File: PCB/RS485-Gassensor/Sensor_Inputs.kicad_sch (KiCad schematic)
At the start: 17 parts, among them SW1 SW_DIP_x06, U3 MQ-6, U8 MQ-6

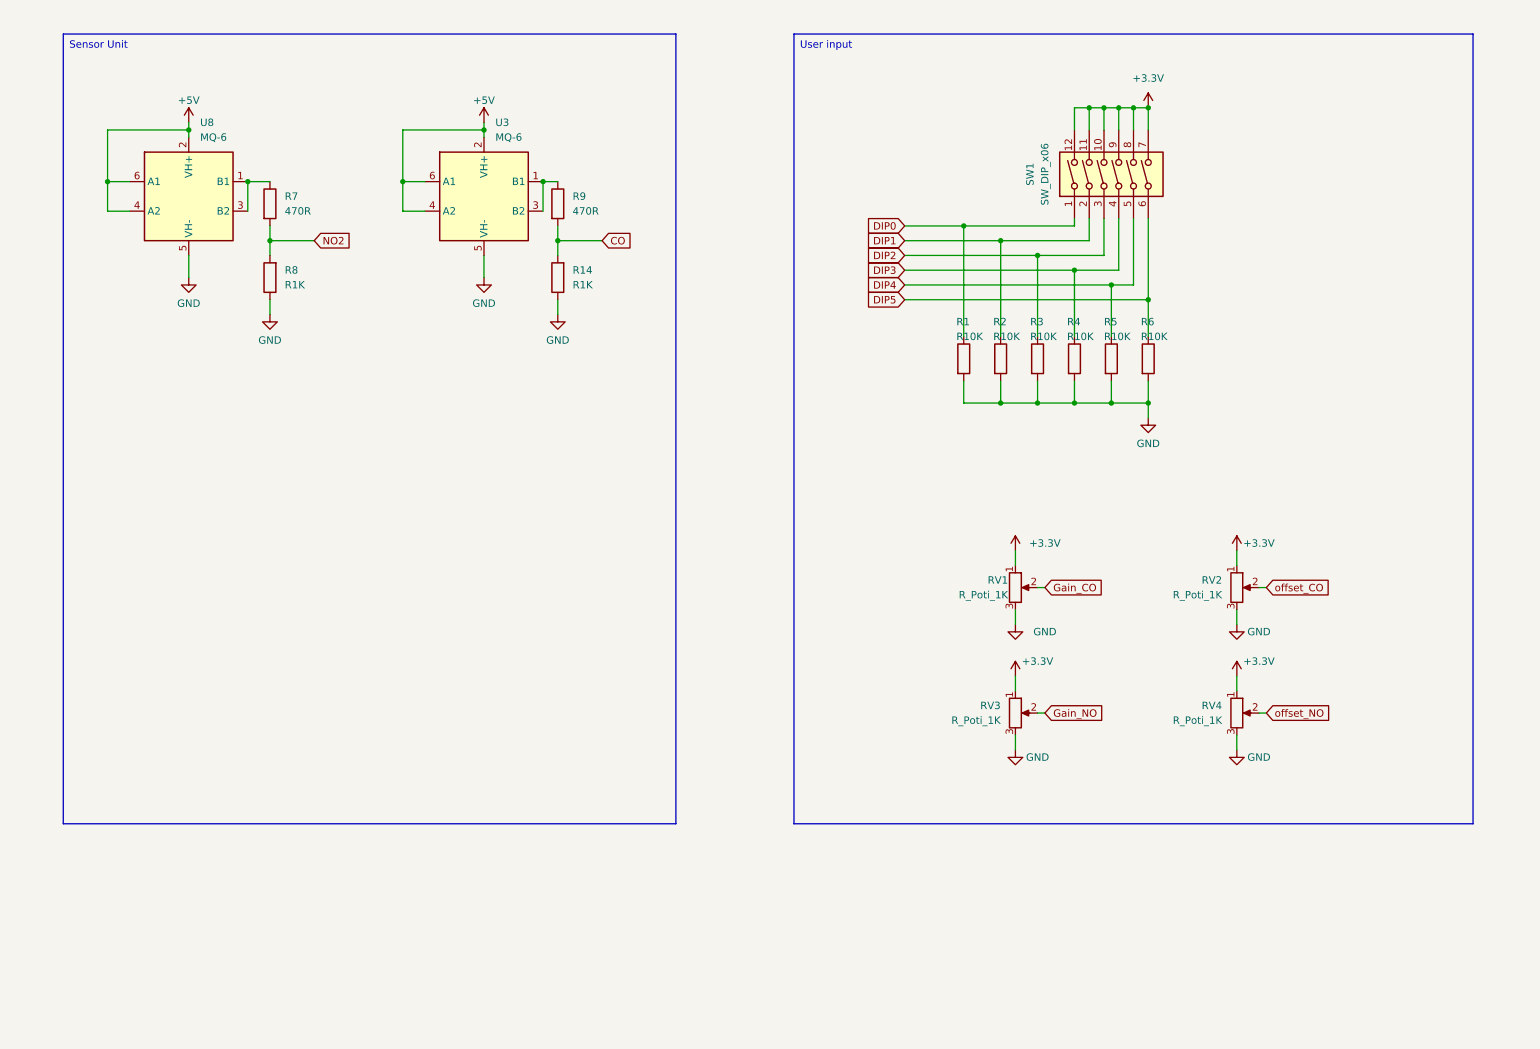
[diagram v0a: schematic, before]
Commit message: added Modbus / RS485
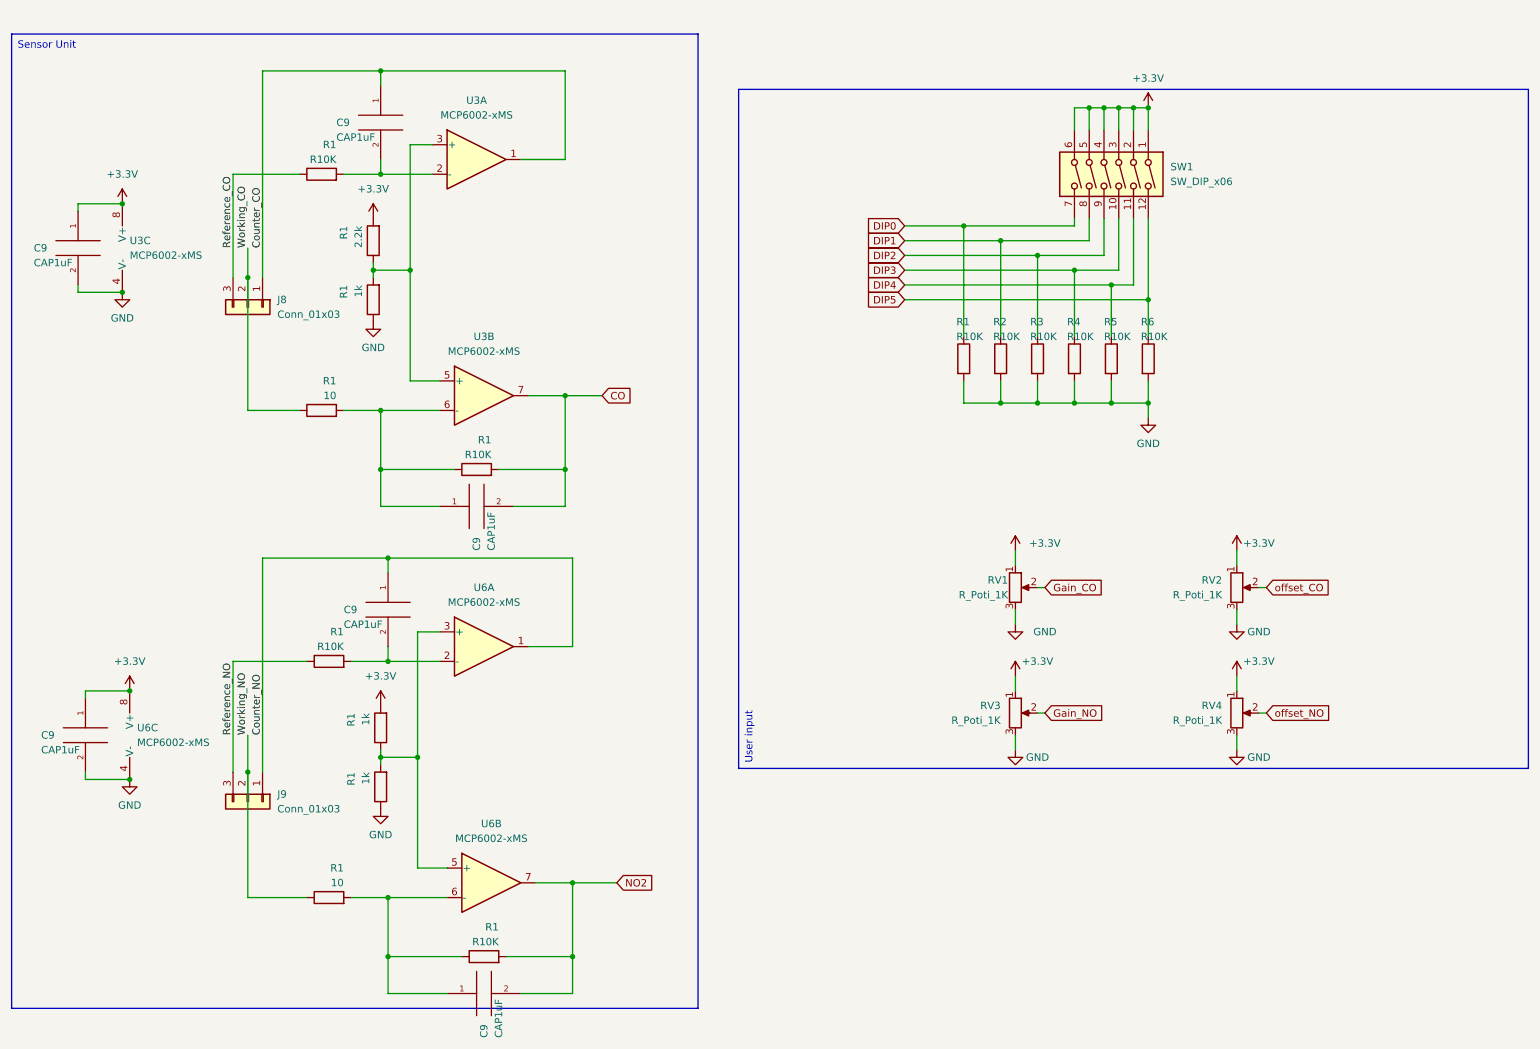
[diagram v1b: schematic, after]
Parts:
- removed R14, R8: R1K, Resistor_SMD:R_0603_1608Metric, symbol Device:R
- removed R7, R9: 470R, Resistor_SMD:R_0603_1608Metric, symbol Device:R
- removed U3, U8: MQ-6, Sensor:MQ-6, symbol Sensor_Gas:MQ-6
- added C9 (x4): CAP1uF, Capacitor_SMD:C_0603_1608Metric, symbol pspice:CAP
- added C9 (x2): CAP1uF, Capacitor_SMD:C_1206_3216Metric, symbol pspice:CAP
- added J8, J9: Conn_01x03, Connector_PinHeader_2.54mm:PinHeader_1x03_P2.54mm_Vertical, symbol Connector_Generic:Conn_01x03
- added R1 (x2): 10, Resistor_SMD:R_0603_1608Metric, symbol Device:R
- added R1 (x3): 1k, Resistor_SMD:R_0603_1608Metric, symbol Device:R
- added R1 (x4): R10K, Resistor_SMD:R_0603_1608Metric, symbol Device:R
- added R1: 2.2k, Resistor_SMD:R_0603_1608Metric, symbol Device:R
- added U3, U6: MCP6002-xMS, Package_SO:SOIC-8_3.9x4.9mm_P1.27mm, symbol Amplifier_Operational:MCP6002-xMS
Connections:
- net +3.3V: now also SW1.1, SW1.2, SW1.3, SW1.4, SW1.5, SW1.6, C9.1, C9.1, R1.2, R1.2, U3.8 (V+), U6.8 (V+); no longer SW1.10, SW1.11, SW1.12, SW1.7, SW1.8, SW1.9
- net CO: now also C9.2, R1.2, U3.7
- net DIP0: now also SW1.7; no longer SW1.1
- net DIP1: now also SW1.8; no longer SW1.2
- net DIP2: now also SW1.9; no longer SW1.3
- net DIP3: now also SW1.10; no longer SW1.4
- net DIP4: now also SW1.11; no longer SW1.5
- net DIP5: now also SW1.12; no longer SW1.6
- net GND: now also C9.2, C9.2, R1.1, R1.1, U3.4 (V-), U6.4 (V-)
- net NO2: now also C9.2, R1.2, U6.7
- new net: C9.1, R1.1, R1.2, U3.6 (-)
- new net: R1.1, R1.2, U3.3 (+), U3.5 (+)
- new net: C9.1, R1.1, R1.2, U6.6 (-)
- new net: C9.2, R1.2, U6.2 (-)
- new net: R1.1, R1.2, U6.3 (+), U6.5 (+)
- new net: C9.2, R1.2, U3.2 (-)
- new net Counter_CO: C9.1, J8.1 (Pin_1), U3.1
- new net Counter_NO: C9.1, J9.1 (Pin_1), U6.1
- new net Reference_CO: J8.3 (Pin_3), R1.1
- new net Reference_NO: J9.3 (Pin_3), R1.1
- new net Working_CO: J8.2 (Pin_2), R1.1
- new net Working_NO: J9.2 (Pin_2), R1.1
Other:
- moved on the sheet: SW1

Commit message: made For NAP505 and NAP550
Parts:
- added C9: CAP100nF, Capacitor_SMD:C_0603_1608Metric, symbol pspice:CAP
- added U8: SHT4x, Sensor_Humidity:Sensirion_DFN-4_1.5x1.5mm_P0.8mm_SHT4x_NoCentralPad, symbol Sensor_Humidity:SHT4x
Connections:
- net +3.3V: now also C9.2, U8.3 (VDD)
- net GND: now also C9.1, U8.4 (VSS)
- new net I2C_SCL: U8.2 (SCL)
- new net I2C_SDA: U8.1 (SDA)
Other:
- moved on the sheet: R1, R2, R3, R4, R5, R6, RV1, RV2, RV3, RV4, SW1
